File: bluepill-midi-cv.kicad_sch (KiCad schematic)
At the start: 97 parts

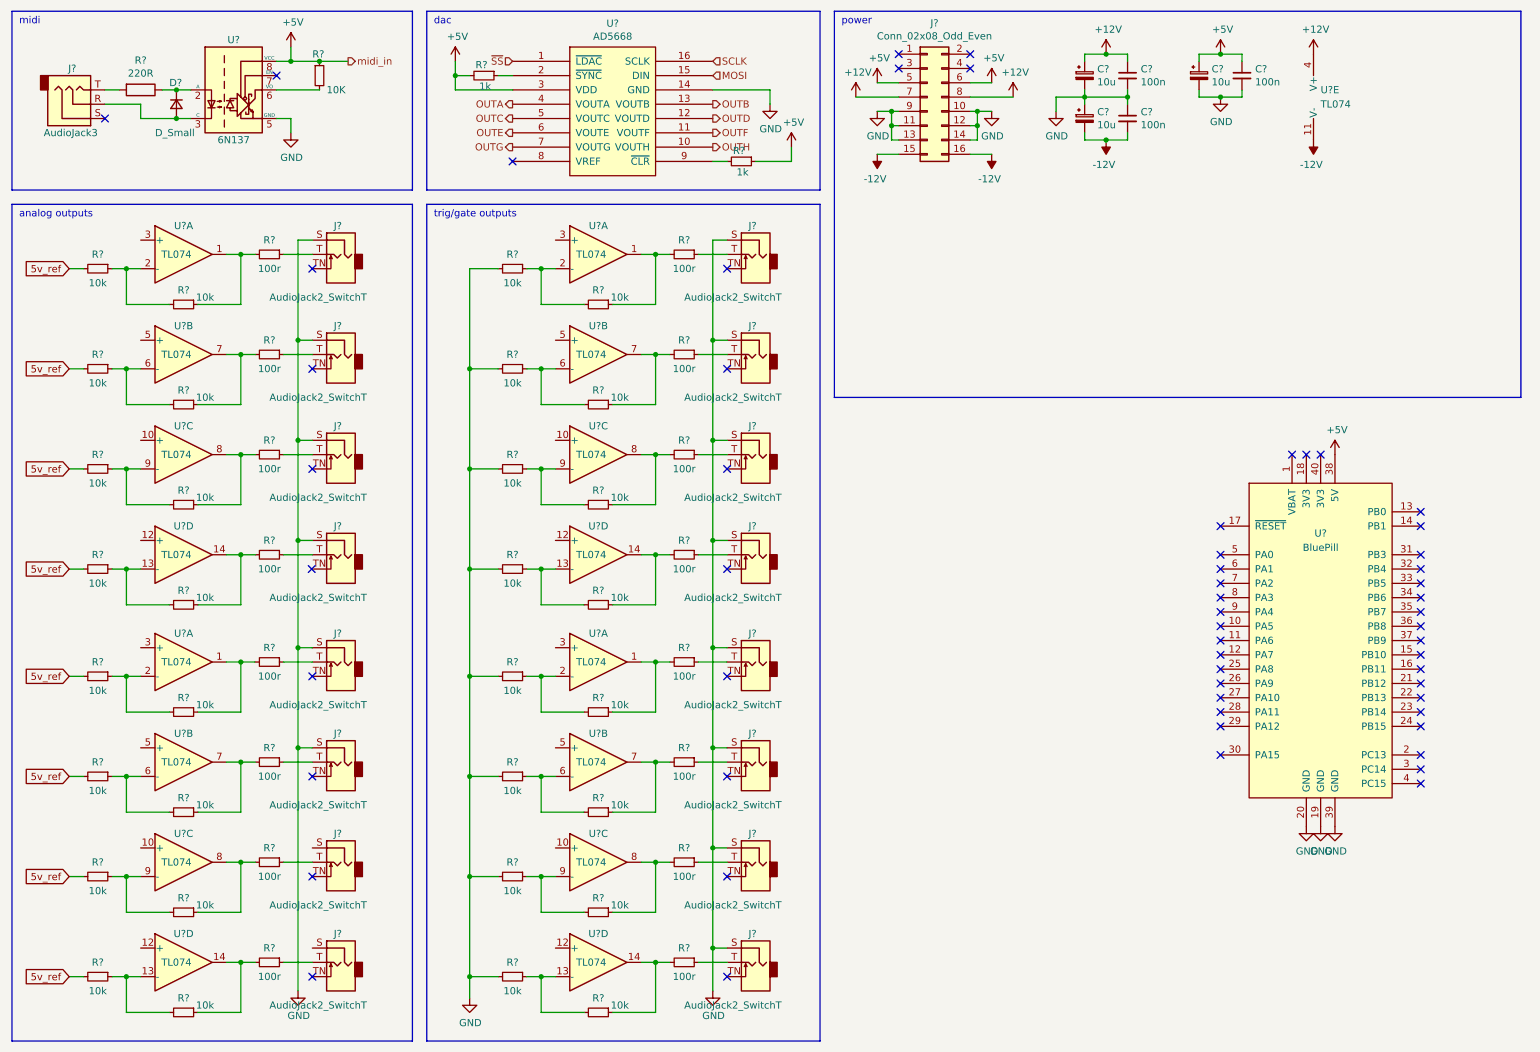
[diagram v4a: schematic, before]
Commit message: fix schgematic labels
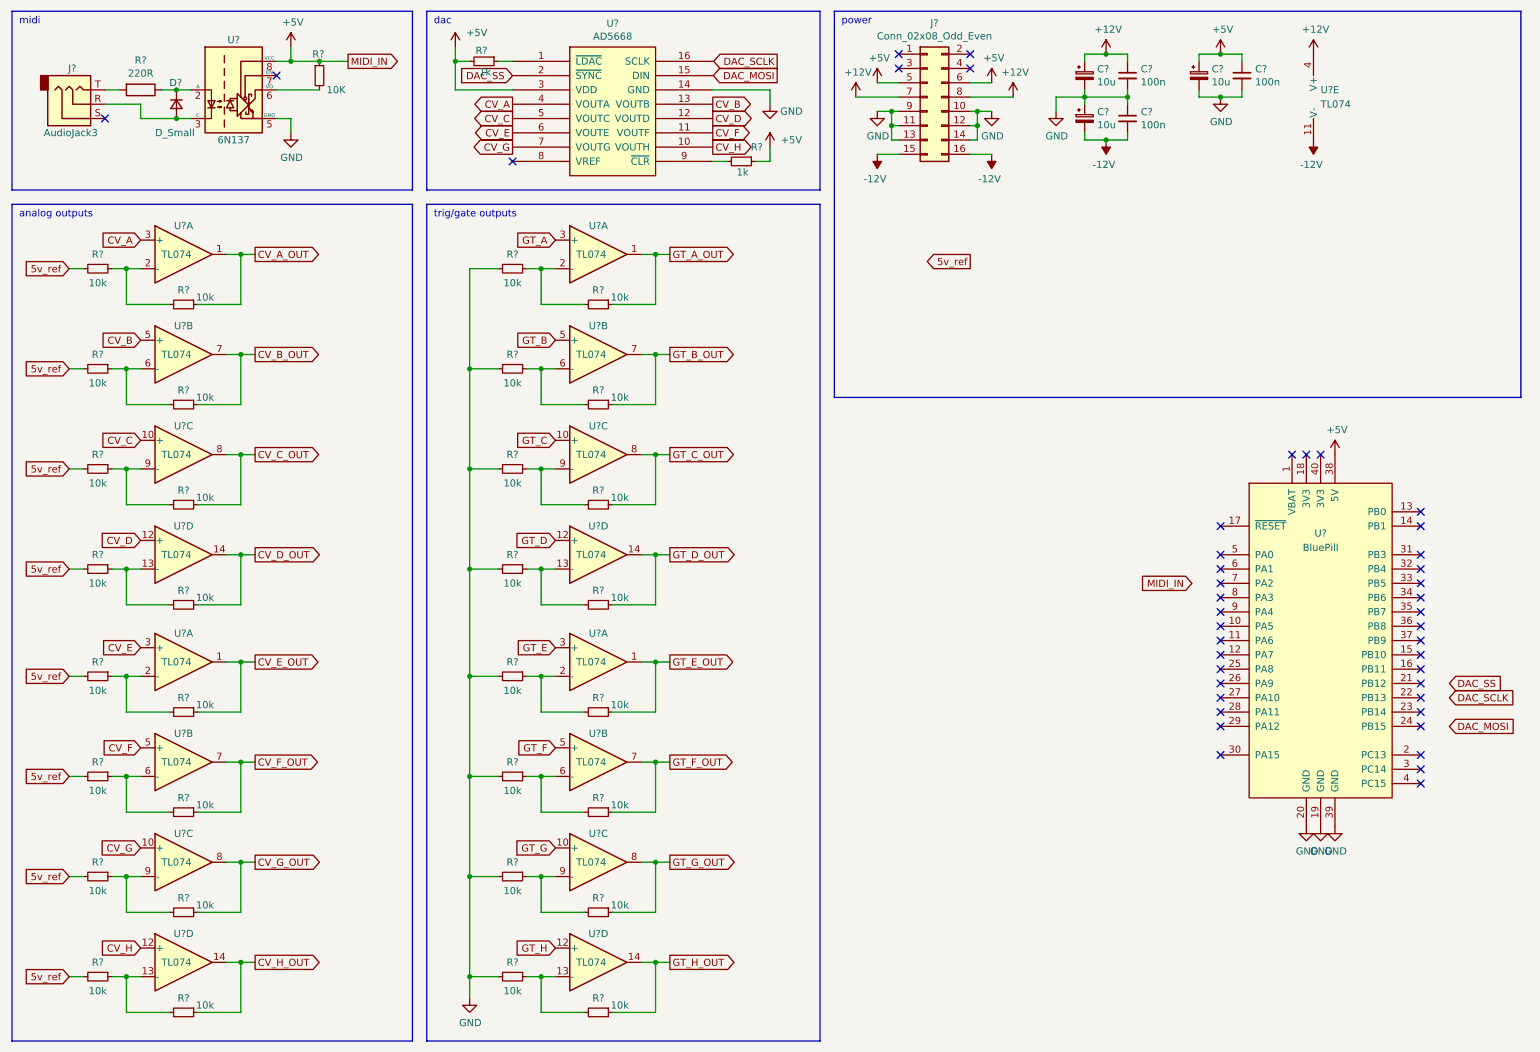
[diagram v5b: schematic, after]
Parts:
- removed J? (x16): AudioJack2_SwitchT, symbol Connector:AudioJack2_SwitchT
- removed R? (x16): 100r, symbol Device:R_Small
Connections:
- net OUTA is gone; now on net CV_A: U?.4 (VOUTA)
- net OUTB is gone; now on net CV_B: U?.13 (VOUTB)
- net OUTC is gone; now on net CV_C: U?.5 (VOUTC)
- net OUTD is gone; now on net CV_D: U?.12 (VOUTD)
- net OUTE is gone; now on net CV_E: U?.6 (VOUTE)
- net OUTF is gone; now on net CV_F: U?.11 (VOUTF)
- net OUTG is gone; now on net CV_G: U?.7 (VOUTG)
- net OUTH is gone; now on net CV_H: U?.10 (VOUTH)
- net ~{SS} is gone; now on an unnamed net: U?.1 (~{LDAC})
- net CV_H_OUT: now reaches R?.1, U?.14
- net CV_A_OUT: now reaches R?.1, U?.1
- net CV_A: now reaches U?.3 (+)
- net GT_H_OUT: now reaches R?.1, U?.14
- net CV_E_OUT: now reaches R?.1, U?.1
- net CV_E: now reaches U?.3 (+)
- net GT_D_OUT: now reaches R?.1, U?.14
- net GT_B_OUT: now reaches R?.1, U?.7
- net GT_G_OUT: now reaches R?.1, U?.8
- net CV_C_OUT: now reaches R?.1, U?.8
- net CV_F_OUT: now reaches R?.1, U?.7
- net GT_E_OUT: now reaches R?.1, U?.1
- net GT_E: now reaches U?.3 (+)
- net at R?.1: no longer U?.2 (~{SYNC})
- net GT_D: now reaches U?.12 (+)
- net GT_A_OUT: now reaches R?.1, U?.1
- net GT_H: now reaches U?.12 (+)
- net CV_D: now reaches U?.12 (+)
- net CV_D_OUT: now reaches R?.1, U?.14
- net CV_B: now reaches U?.5 (+)
- net CV_B_OUT: now reaches R?.1, U?.7
- net GT_B: now reaches U?.5 (+)
- net CV_G_OUT: now reaches R?.1, U?.8
- net GT_C_OUT: now reaches R?.1, U?.8
- net GT_G: now reaches U?.10 (+)
- net CV_F: now reaches U?.5 (+)
- net GT_F_OUT: now reaches R?.1, U?.7
- net GT_C: now reaches U?.10 (+)
- net CV_H: now reaches U?.12 (+)
- net CV_G: now reaches U?.10 (+)
- net GT_A: now reaches U?.3 (+)
- net GT_F: now reaches U?.5 (+)
- net CV_C: now reaches U?.10 (+)
- net MOSI: no longer names the net of U?.15 (DIN)
- net SCLK: no longer names the net of U?.16 (SCLK)
- new net DAC_SS: U?.2 (~{SYNC})
- no-connect marks 59 -> 43
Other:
- moved on the sheet: R?

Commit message: schematic cleanup
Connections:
- net CV_E_OUT: no longer R?.1
- net at R?.1, U?.2 (-): no longer R?.2
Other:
- moved on the sheet: R?

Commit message: schema: add board-to-board connectors
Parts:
- added J? (x2): Conn_02x08_Counter_Clockwise, symbol Connector_Generic:Conn_02x08_Counter_Clockwise
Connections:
- net CV_A_OUT: now also J?.2 (Pin_2)
- net CV_B_OUT: now also J?.15 (Pin_15)
- net CV_C_OUT: now also J?.4 (Pin_4)
- net CV_D_OUT: now also J?.13 (Pin_13)
- net CV_E_OUT: now also J?.6 (Pin_6)
- net CV_F_OUT: now also J?.11 (Pin_11)
- net CV_G_OUT: now also J?.8 (Pin_8)
- net CV_H_OUT: now also J?.9 (Pin_9)
- net GND: now also J?.1 (Pin_1), J?.10 (Pin_10), J?.10 (Pin_10), J?.12 (Pin_12), J?.12 (Pin_12), J?.14 (Pin_14), J?.14 (Pin_14), J?.16 (Pin_16), J?.3 (Pin_3), J?.3 (Pin_3), J?.5 (Pin_5), J?.5 (Pin_5), J?.7 (Pin_7), J?.7 (Pin_7)
- net GT_A_OUT: now also J?.2 (Pin_2)
- net GT_B_OUT: now also J?.15 (Pin_15)
- net GT_C_OUT: now also J?.4 (Pin_4)
- net GT_D_OUT: now also J?.13 (Pin_13)
- net GT_E_OUT: now also J?.6 (Pin_6)
- net GT_F_OUT: now also J?.11 (Pin_11)
- net GT_G_OUT: now also J?.8 (Pin_8)
- net GT_H_OUT: now also J?.9 (Pin_9)
- new net MIDI+: J?.1 (Pin_1)
- new net MIDI-: J?.16 (Pin_16)

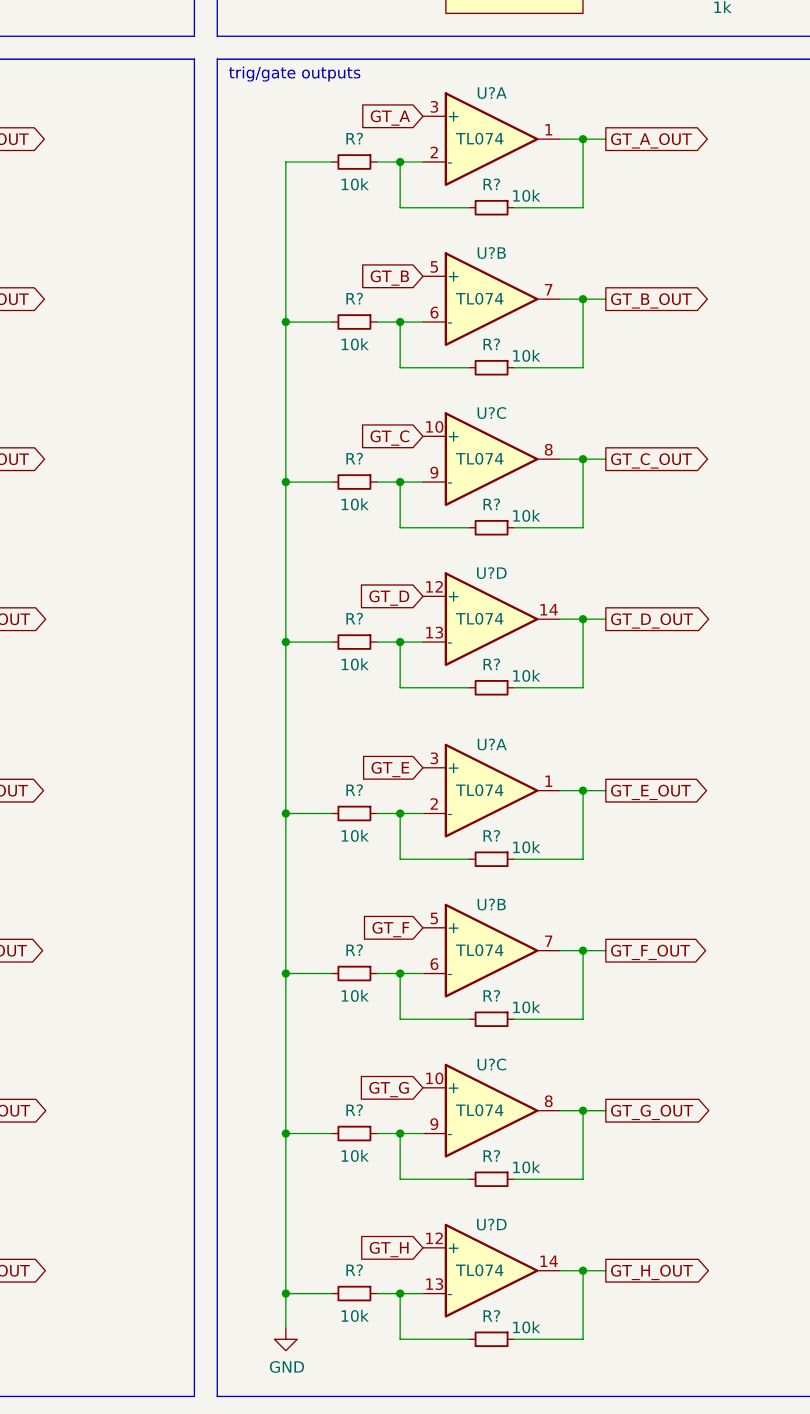
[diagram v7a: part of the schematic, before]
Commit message: fix gain for gate outputs
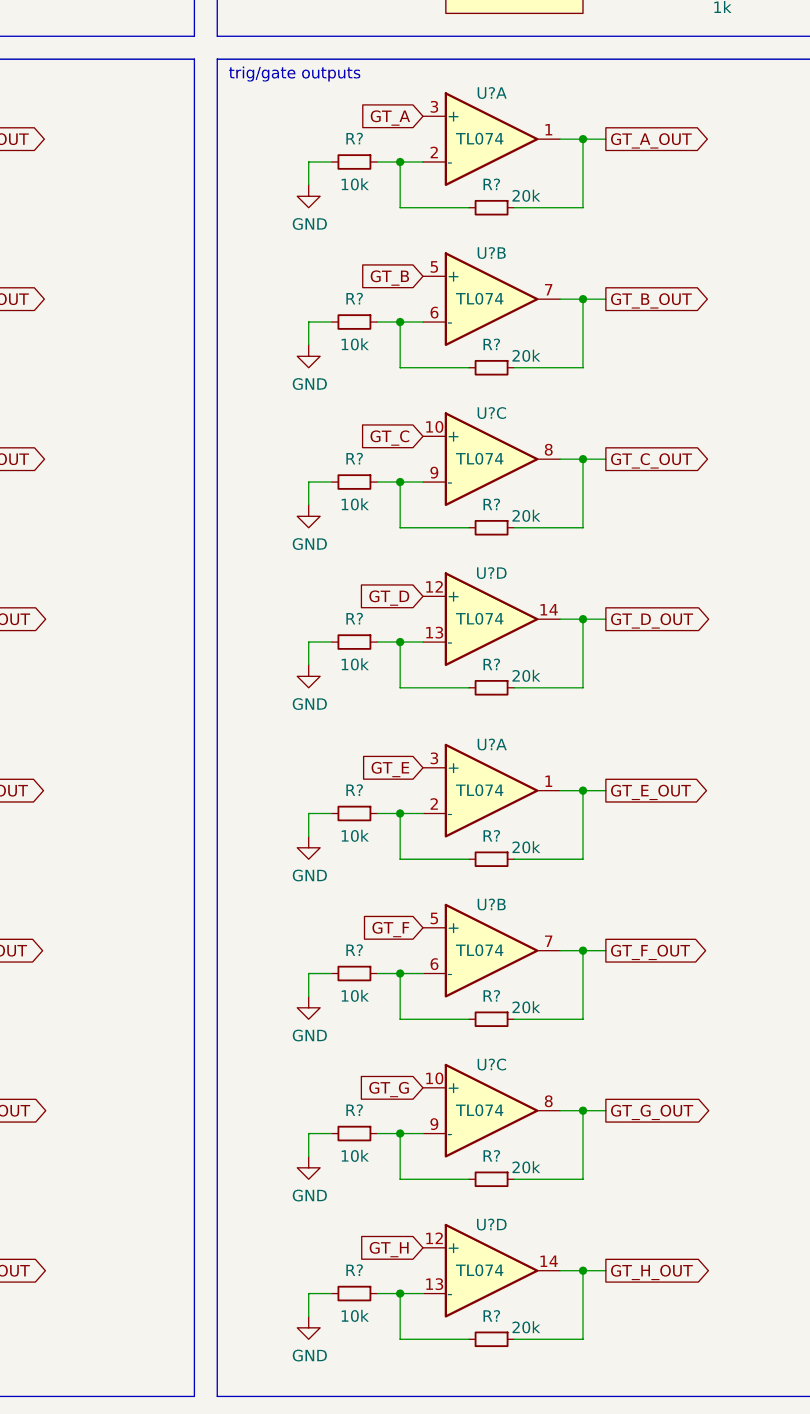
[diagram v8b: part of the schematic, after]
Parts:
- R? (x8): value 10k -> 20k
